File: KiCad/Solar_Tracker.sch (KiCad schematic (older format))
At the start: 24 parts

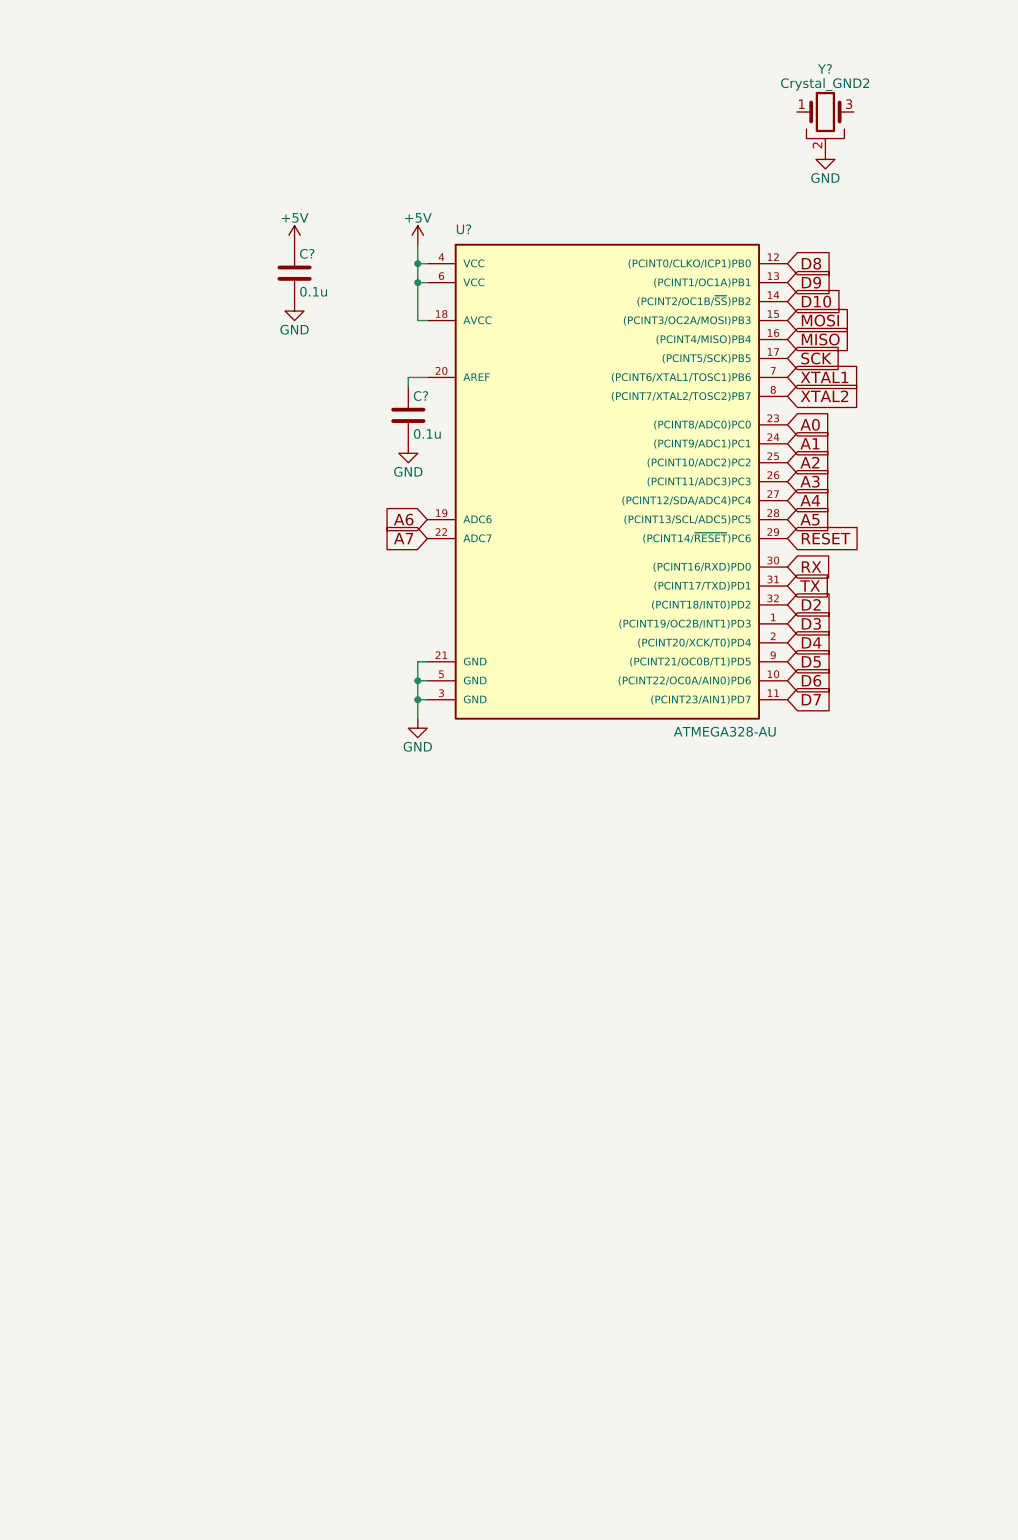
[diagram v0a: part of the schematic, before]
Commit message: Added FTDI chip to library, added Atmega328 to schematic
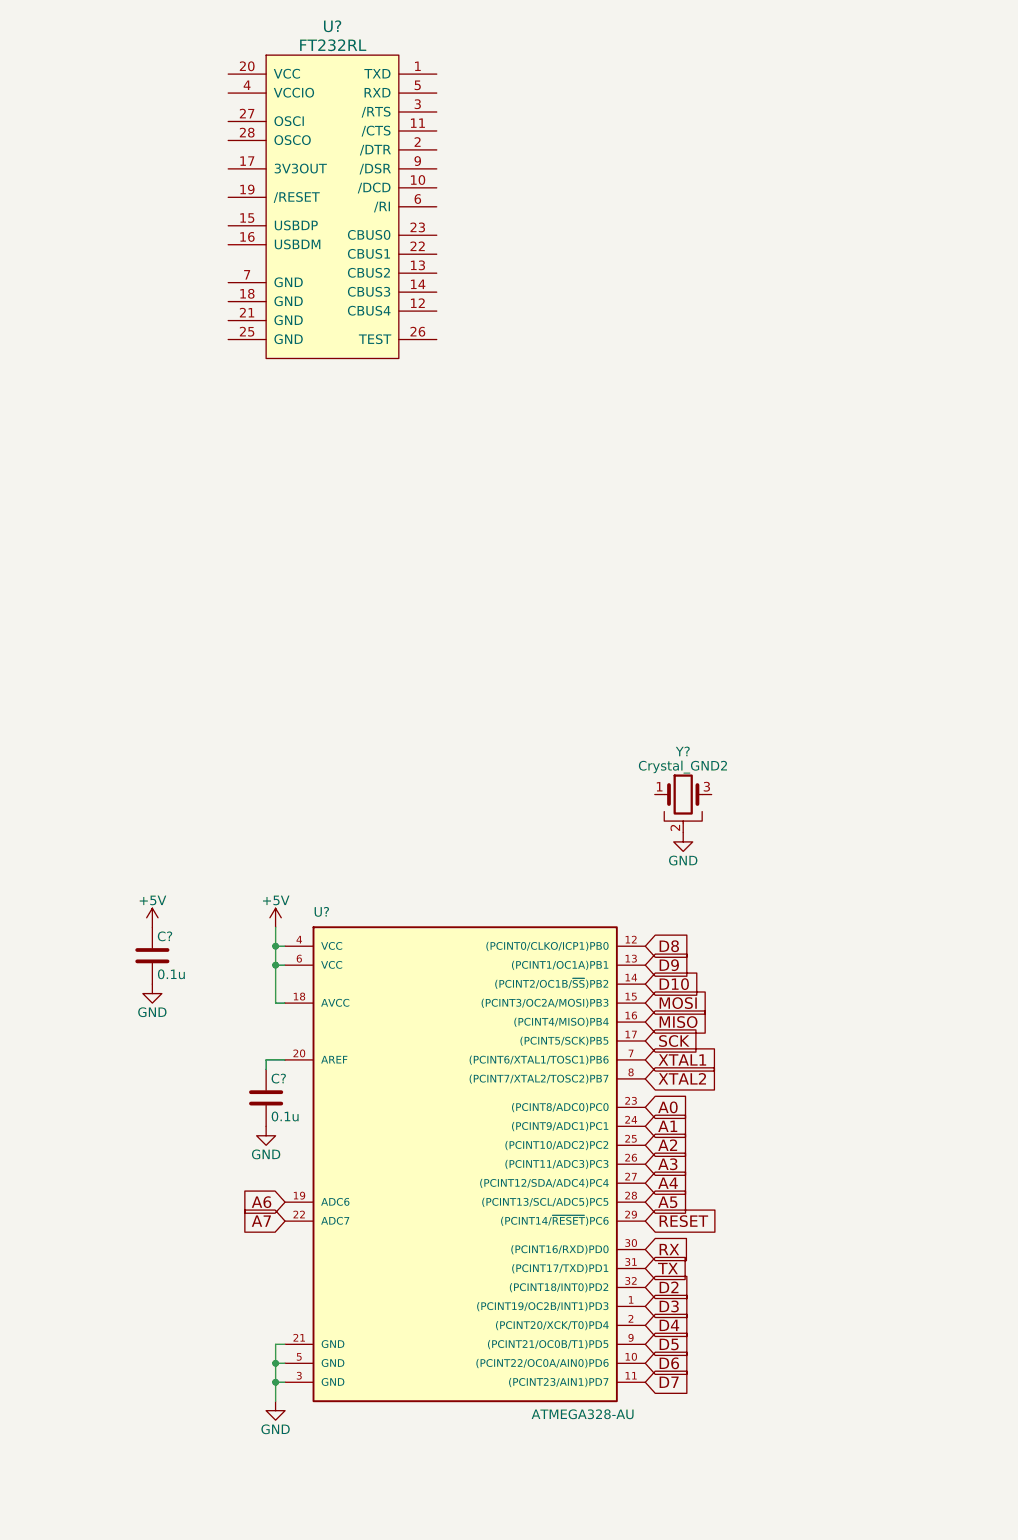
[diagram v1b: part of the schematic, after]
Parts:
- added U?: FT232RL, symbol FT232RL
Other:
- moved on the sheet: C?, U?, Y?
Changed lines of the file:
@@
 L ATMEGA328-AU U?
 U 1 1 59C40244
-P 4850 3700
-F 0 "U?" H 4100 4950 50  0000 L BNN
-F 1 "ATMEGA328-AU" H 5250 2300 50  0000 L BNN
-F 2 "TQFP32" H 4850 3700 50  0001 C CIN
-F 3 "" H 4850 3700 50  0001 C CNN
-	1    4850 3700
+P 4100 7300
+F 0 "U?" H 3350 8550 50  0000 L BNN
+F 1 "ATMEGA328-AU" H 4500 5900 50  0000 L BNN
+F 2 "TQFP32" H 4100 7300 50  0001 C CIN
+F 3 "" H 4100 7300 50  0001 C CNN
+	1    4100 7300
 	1    0    0    -1
 $EndComp
@@
 L +5V #PWR?
 U 1 1 59C4066F
-P 3900 2500
-F 0 "#PWR?" H 3900 2350 50  0001 C CNN
-F 1 "+5V" H 3900 2640 50  0000 C CNN
-F 2 "" H 3900 2500 50  0001 C CNN
-F 3 "" H 3900 2500 50  0001 C CNN
-	1    3900 2500
+P 3150 6100
+F 0 "#PWR?" H 3150 5950 50  0001 C CNN
+F 1 "+5V" H 3150 6240 50  0000 C CNN
+F 2 "" H 3150 6100 50  0001 C CNN
+F 3 "" H 3150 6100 50  0001 C CNN
+	1    3150 6100
 	1    0    0    -1
 $EndComp
@@
 L C C?
 U 1 1 59C40FCA
-P 3250 2650
-F 0 "C?" H 3275 2750 50  0000 L CNN
-F 1 "0.1u" H 3275 2550 50  0000 L CNN
-F 2 "" H 3288 2500 50  0001 C CNN
-F 3 "" H 3250 2650 50  0001 C CNN
-	1    3250 2650
+P 2500 6250
+F 0 "C?" H 2525 6350 50  0000 L CNN
+F 1 "0.1u" H 2525 6150 50  0000 L CNN
+F 2 "" H 2538 6100 50  0001 C CNN
+F 3 "" H 2500 6250 50  0001 C CNN
+	1    2500 6250
 	1    0    0    -1
 $EndComp
@@
 L C C?
 U 1 1 59C410D1
-P 3850 3400
-F 0 "C?" H 3875 3500 50  0000 L CNN
-F 1 "0.1u" H 3875 3300 50  0000 L CNN
-F 2 "" H 3888 3250 50  0001 C CNN
-F 3 "" H 3850 3400 50  0001 C CNN
-	1    3850 3400
+P 3100 7000
+F 0 "C?" H 3125 7100 50  0000 L CNN
+F 1 "0.1u" H 3125 6900 50  0000 L CNN
+F 2 "" H 3138 6850 50  0001 C CNN
+F 3 "" H 3100 7000 50  0001 C CNN
+	1    3100 7000
 	1    0    0    -1
 $EndComp
@@
 L GND #PWR?
 U 1 1 59C41BC8
-P 3900 5000
-F 0 "#PWR?" H 3900 4750 50  0001 C CNN
-F 1 "GND" H 3900 4850 50  0000 C CNN
-F 2 "" H 3900 5000 50  0001 C CNN
-F 3 "" H 3900 5000 50  0001 C CNN
-	1    3900 5000
+P 3150 8600
+F 0 "#PWR?" H 3150 8350 50  0001 C CNN
+F 1 "GND" H 3150 8450 50  0000 C CNN
+F 2 "" H 3150 8600 50  0001 C CNN
+F 3 "" H 3150 8600 50  0001 C CNN
+	1    3150 8600
 	1    0    0    -1
 $EndComp
@@
 	10100 7100 10100 7450
 Wire Wire Line
-	3900 2500 3900 2600
-Wire Wire Line
-	3900 2600 3900 2700
-Wire Wire Line
-	3900 2700 3900 2900
-Wire Wire Line
-	3900 2900 3950 2900
-Wire Wire Line
-	3950 2600 3900 2600
-Connection ~ 3900 2600
-Wire Wire Line
-	3950 2700 3900 2700
-Connection ~ 3900 2700
-Wire Wire Line
-	3950 4700 3900 4700
-Wire Wire Line
-	3900 4700 3900 4800
-Wire Wire Line
-	3900 4800 3900 4900
-Wire Wire Line
-	3900 4900 3900 5000
-Wire Wire Line
-	3950 4800 3900 4800
-Connection ~ 3900 4800
-Wire Wire Line
-	3950 4900 3900 4900
-Connection ~ 3900 4900
+	3150 6100 3150 6200
+Wire Wire Line
+	3150 6200 3150 6300
+Wire Wire Line
+	3150 6300 3150 6500
+Wire Wire Line
+	3150 6500 3200 6500
+Wire Wire Line
+	3200 6200 3150 6200
+Connection ~ 3150 6200
+Wire Wire Line
+	3200 6300 3150 6300
+Connection ~ 3150 6300
+Wire Wire Line
+	3200 8300 3150 8300
+Wire Wire Line
+	3150 8300 3150 8400
+Wire Wire Line
+	3150 8400 3150 8500
+Wire Wire Line
+	3150 8500 3150 8600
+Wire Wire Line
+	3200 8400 3150 8400
+Connection ~ 3150 8400
+Wire Wire Line
+	3200 8500 3150 8500
+Connection ~ 3150 8500
 $Comp
 L +5V #PWR?
 U 1 1 59C42053
-P 3250 2500
-F 0 "#PWR?" H 3250 2350 50  0001 C CNN
-F 1 "+5V" H 3250 2640 50  0000 C CNN
-F 2 "" H 3250 2500 50  0001 C CNN
-F 3 "" H 3250 2500 50  0001 C CNN
-	1    3250 2500
+P 2500 6100
+F 0 "#PWR?" H 2500 5950 50  0001 C CNN
+F 1 "+5V" H 2500 6240 50  0000 C CNN
+F 2 "" H 2500 6100 50  0001 C CNN
+F 3 "" H 2500 6100 50  0001 C CNN
+	1    2500 6100
 	1    0    0    -1
 $EndComp
@@
 L GND #PWR?
 U 1 1 59C420A9
-P 3250 2800
-F 0 "#PWR?" H 3250 2550 50  0001 C CNN
-F 1 "GND" H 3250 2650 50  0000 C CNN
-F 2 "" H 3250 2800 50  0001 C CNN
-F 3 "" H 3250 2800 50  0001 C CNN
-	1    3250 2800
+P 2500 6400
+F 0 "#PWR?" H 2500 6150 50  0001 C CNN
+F 1 "GND" H 2500 6250 50  0000 C CNN
+F 2 "" H 2500 6400 50  0001 C CNN
+F 3 "" H 2500 6400 50  0001 C CNN
+	1    2500 6400
 	1    0    0    -1
 $EndComp
@@
 L GND #PWR?
 U 1 1 59C420E9
-P 3850 3550
-F 0 "#PWR?" H 3850 3300 50  0001 C CNN
-F 1 "GND" H 3850 3400 50  0000 C CNN
-F 2 "" H 3850 3550 50  0001 C CNN
-F 3 "" H 3850 3550 50  0001 C CNN
-	1    3850 3550
-	1    0    0    -1
-$EndComp
-Wire Wire Line
-	3950 3200 3850 3200
-Wire Wire Line
-	3850 3200 3850 3250
+P 3100 7150
+F 0 "#PWR?" H 3100 6900 50  0001 C CNN
+F 1 "GND" H 3100 7000 50  0000 C CNN
+F 2 "" H 3100 7150 50  0001 C CNN
+F 3 "" H 3100 7150 50  0001 C CNN
+	1    3100 7150
+	1    0    0    -1
+$EndComp
+Wire Wire Line
+	3200 6800 3100 6800
+Wire Wire Line
+	3100 6800 3100 6850
 $Comp
 L Crystal_GND2 Y?
 U 1 1 59C423FF
-P 6050 1800
-F 0 "Y?" H 6050 2025 50  0000 C CNN
-F 1 "Crystal_GND2" H 6050 1950 50  0000 C CNN
-F 2 "" H 6050 1800 50  0001 C CNN
-F 3 "" H 6050 1800 50  0001 C CNN
-	1    6050 1800
+P 5300 5400
+F 0 "Y?" H 5300 5625 50  0000 C CNN
+F 1 "Crystal_GND2" H 5300 5550 50  0000 C CNN
+F 2 "" H 5300 5400 50  0001 C CNN
+F 3 "" H 5300 5400 50  0001 C CNN
+	1    5300 5400
 	1    0    0    -1
 $EndComp
@@
 L GND #PWR?
 U 1 1 59C4248C
-P 6050 2000
-F 0 "#PWR?" H 6050 1750 50  0001 C CNN
-F 1 "GND" H 6050 1850 50  0000 C CNN
-F 2 "" H 6050 2000 50  0001 C CNN
-F 3 "" H 6050 2000 50  0001 C CNN
-	1    6050 2000
-	1    0    0    -1
-$EndComp
-Text GLabel 5850 3200 2    60   Input ~ 0
+P 5300 5600
+F 0 "#PWR?" H 5300 5350 50  0001 C CNN
+F 1 "GND" H 5300 5450 50  0000 C CNN
+F 2 "" H 5300 5600 50  0001 C CNN
+F 3 "" H 5300 5600 50  0001 C CNN
+	1    5300 5600
+	1    0    0    -1
+$EndComp
+Text GLabel 5100 6800 2    60   Input ~ 0
 XTAL1
-Text GLabel 5850 3300 2    60   Input ~ 0
+Text GLabel 5100 6900 2    60   Input ~ 0
 XTAL2
-Text GLabel 5850 4200 2    60   Input ~ 0
+Text GLabel 5100 7800 2    60   Input ~ 0
 RX
-Text GLabel 5850 4300 2    60   Input ~ 0
+Text GLabel 5100 7900 2    60   Input ~ 0
 TX
-Text GLabel 5850 2900 2    60   Input ~ 0
+Text GLabel 5100 6500 2    60   Input ~ 0
 MOSI
-Text GLabel 5850 3000 2    60   Input ~ 0
+Text GLabel 5100 6600 2    60   Input ~ 0
 MISO
-Text GLabel 5850 3100 2    60   Input ~ 0
+Text GLabel 5100 6700 2    60   Input ~ 0
 SCK
-Text GLabel 5850 4050 2    60   Input ~ 0
+Text GLabel 5100 7650 2    60   Input ~ 0
 RESET
-Text GLabel 5850 2600 2    60   Input ~ 0
+Text GLabel 5100 6200 2    60   Input ~ 0
 D8
-Text GLabel 5850 2700 2    60   Input ~ 0
+Text GLabel 5100 6300 2    60   Input ~ 0
 D9
-Text GLabel 5850 2800 2    60   Input ~ 0
+Text GLabel 5100 6400 2    60   Input ~ 0
 D10
-Text GLabel 5850 3450 2    60   Input ~ 0
+Text GLabel 5100 7050 2    60   Input ~ 0
 A0
-Text GLabel 5850 3550 2    60   Input ~ 0
+Text GLabel 5100 7150 2    60   Input ~ 0
 A1
-Text GLabel 5850 3650 2    60   Input ~ 0
+Text GLabel 5100 7250 2    60   Input ~ 0
 A2
-Text GLabel 5850 3750 2    60   Input ~ 0
+Text GLabel 5100 7350 2    60   Input ~ 0
 A3
-Text GLabel 5850 3850 2    60   Input ~ 0
+Text GLabel 5100 7450 2    60   Input ~ 0
 A4
-Text GLabel 5850 3950 2    60   Input ~ 0
+Text GLabel 5100 7550 2    60   Input ~ 0
 A5
-Text GLabel 5850 4400 2    60   Input ~ 0
+Text GLabel 5100 8000 2    60   Input ~ 0
 D2
-Text GLabel 5850 4500 2    60   Input ~ 0
+Text GLabel 5100 8100 2    60   Input ~ 0
 D3
-Text GLabel 5850 4600 2    60   Input ~ 0
+Text GLabel 5100 8200 2    60   Input ~ 0
 D4
-Text GLabel 5850 4700 2    60   Input ~ 0
+Text GLabel 5100 8300 2    60   Input ~ 0
 D5
-Text GLabel 5850 4800 2    60   Input ~ 0
+Text GLabel 5100 8400 2    60   Input ~ 0
 D6
-Text GLabel 5850 4900 2    60   Input ~ 0
+Text GLabel 5100 8500 2    60   Input ~ 0
 D7
-Text GLabel 3950 3950 0    60   Input ~ 0
+Text GLabel 3200 7550 0    60   Input ~ 0
 A6
-Text GLabel 3950 4050 0    60   Input ~ 0
+Text GLabel 3200 7650 0    60   Input ~ 0
 A7
 $Comp
@@
 	1    0    0    -1
 $EndComp
+$Comp
+L FT232RL U?
+U 1 1 59C423C3
+P 3450 2200
+F 0 "U?" H 3450 3050 60  0000 C CNN
+F 1 "FT232RL" H 3450 2950 60  0000 C CNN
+F 2 "" H 3450 2200 60  0001 C CNN
+F 3 "" H 3450 2200 60  0001 C CNN
+	1    3450 2200
+	1    0    0    -1
+$EndComp

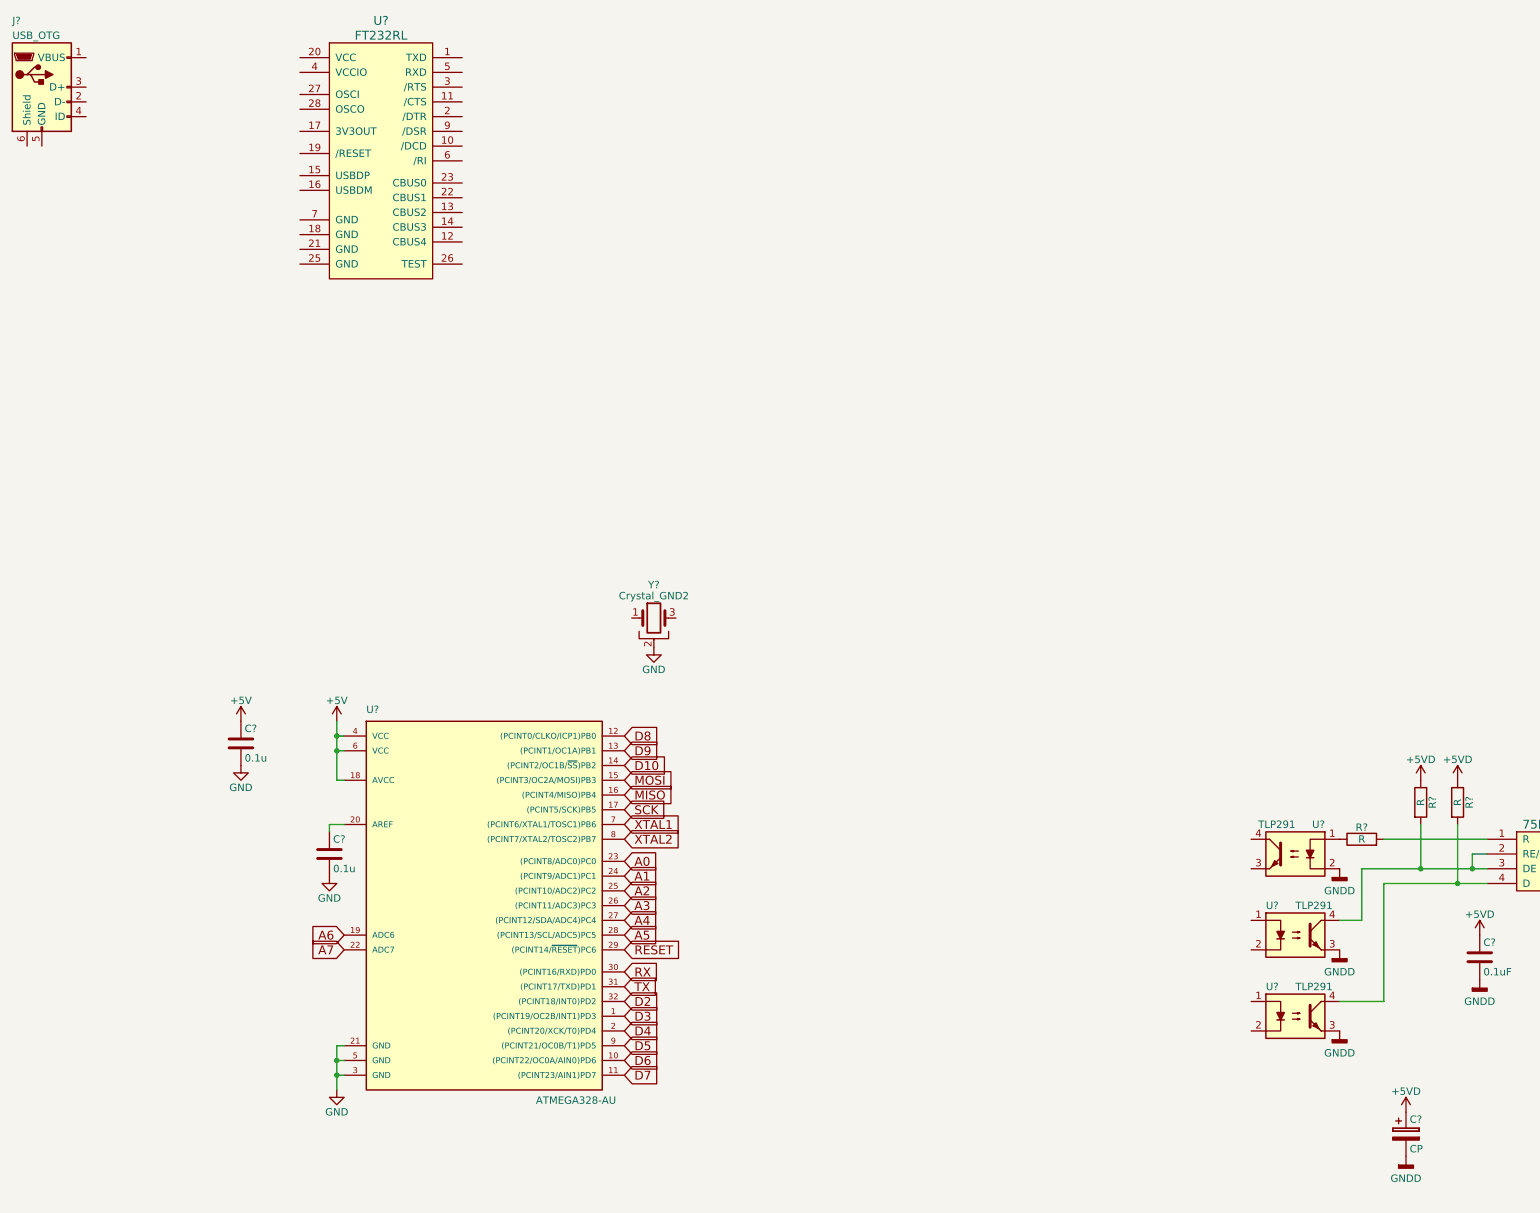
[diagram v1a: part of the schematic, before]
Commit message: added connections to FTDI chip
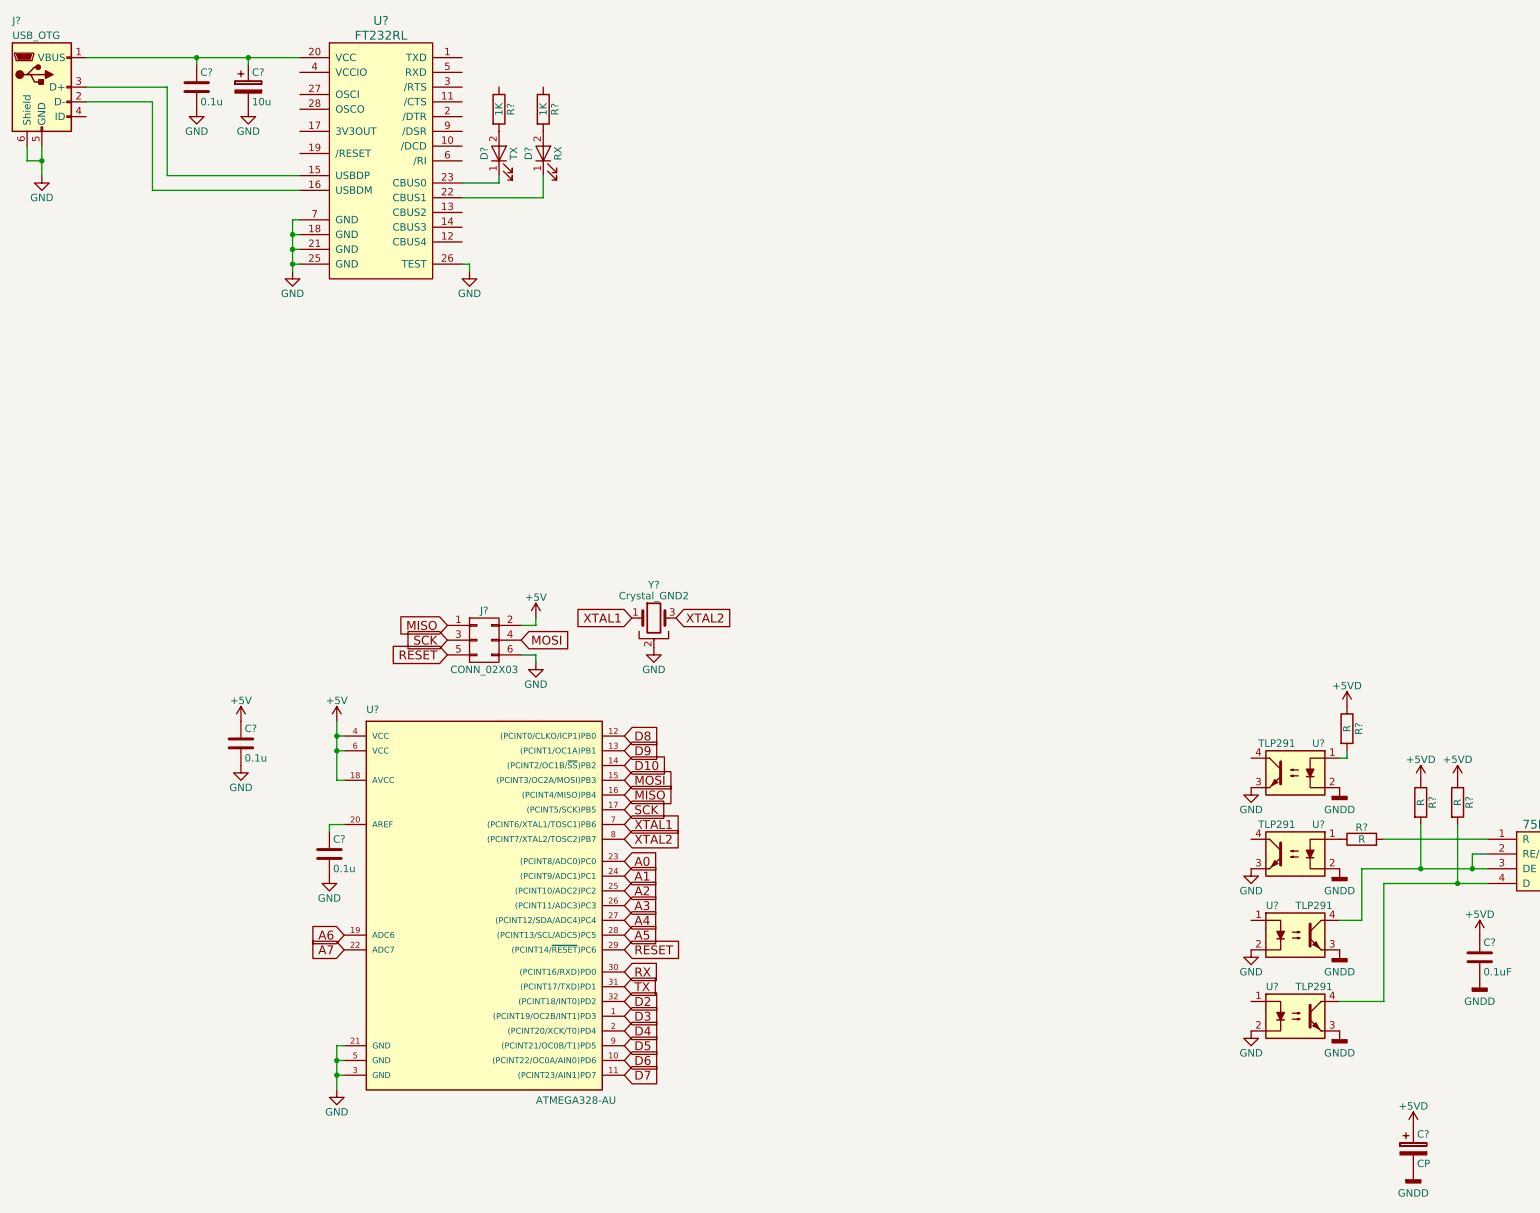
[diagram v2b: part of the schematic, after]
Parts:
- added C?: 10u, symbol CP
- added C?: 0.1u, symbol C
- added D?: TX, symbol LED
- added D?: RX, symbol LED
- added J?: CONN_02X03, symbol CONN_02X03
- added R? (x2): 1K, symbol R
- added R?: R, symbol R
- added U?: TLP291, Housings_DIP:DIP-4_W7.62mm_SMD, symbol TLP291
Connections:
- wire segments 63 -> 98
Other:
- moved on the sheet: C?
